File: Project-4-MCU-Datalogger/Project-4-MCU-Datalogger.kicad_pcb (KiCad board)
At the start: 2 copper layers, 51.9 x 33.4 mm, 30 parts, among them J1 Conn_01x04_Pin, J2 Conn_01x04_Pin, J3 Conn_01x09_Pin, J4 Conn_02x03_Odd_Even, U1 24LC1025, U2 24LC1025, U3 DS1337S_, U4 ATMEGA328P-AU, Y1 16 MHz, Y2 32.768 KHz

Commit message: bugfix I2C's clock signal updating routing after schematic bugfix of net label (rename from SCK to SCL)
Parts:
- removed REF**: KiCad-Logo2_5mm_SilkScreen, Symbol:KiCad-Logo2_5mm_SilkScreen
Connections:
- J1 pad 4: /SCK -> /SCL
- R3 pad 2: /SCK -> /SCL
- U1 pad 6: /SCK -> /SCL
- U2 pad 6: /SCK -> /SCL
- U3 pad 6: /SCK -> /SCL
- U4 pad 28: /SCK -> /SCL
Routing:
- net /SCL: track 0.00 -> 68.7 mm, vias 0 -> 6
- net /SCK: track 80.0 -> 16.2 mm, vias 9 -> 2
- net /SDA: track 64.0 -> 63.0 mm

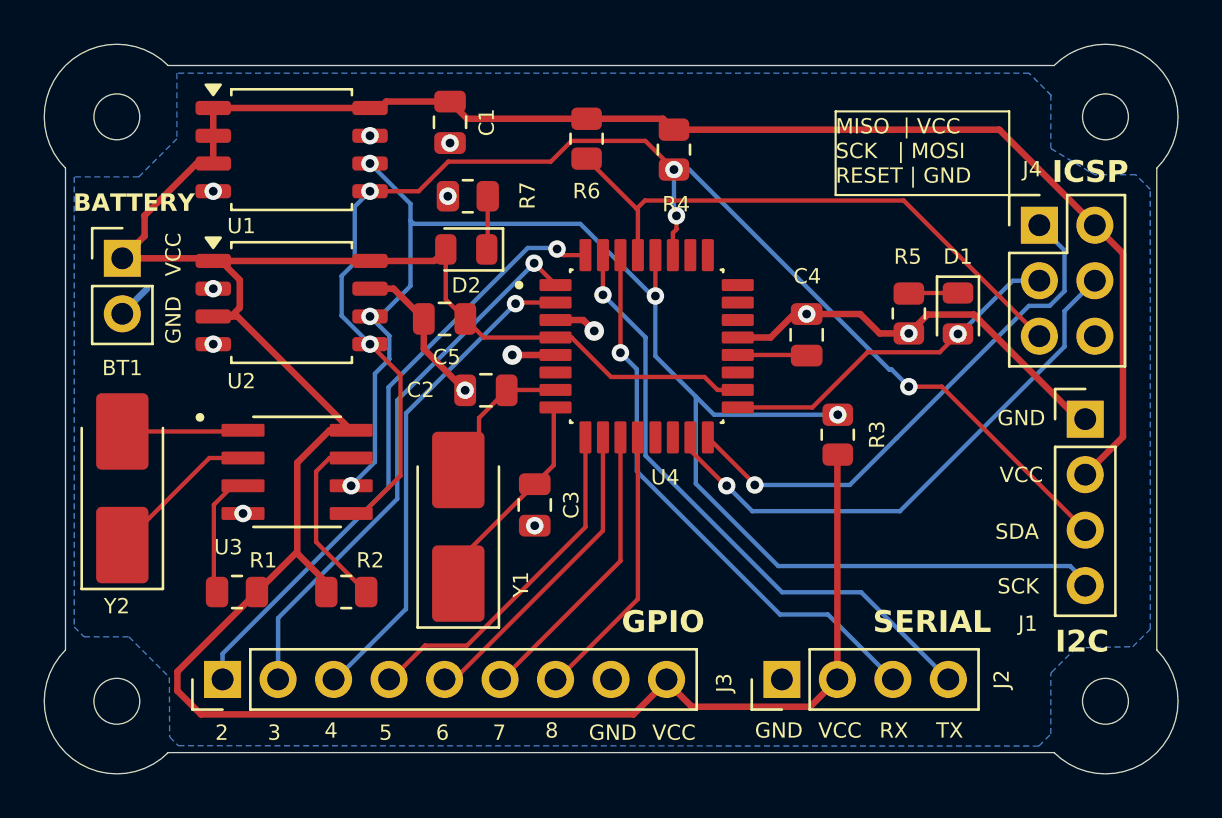
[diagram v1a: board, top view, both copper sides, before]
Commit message: delete all zones, tracks, vias before autorouting
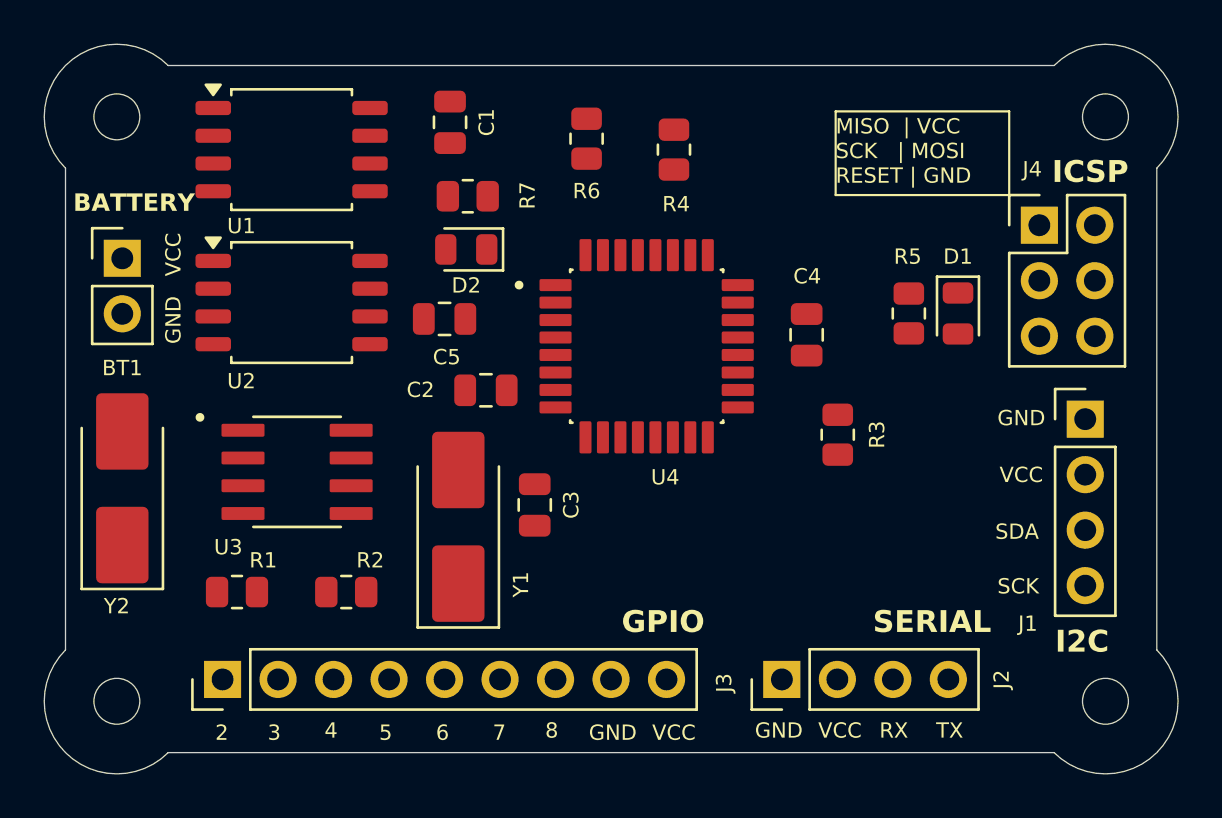
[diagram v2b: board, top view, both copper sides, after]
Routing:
- net /Vcc: track 171.1 -> 0.00 mm
- net /SCL: track 68.7 -> 0.00 mm, vias 6 -> 0
- net /SDA: track 63.0 -> 0.00 mm, vias 5 -> 0
- net GND: track 31.8 -> 0.00 mm, vias 18 -> 0
- net /D2: track 28.4 -> 0.00 mm, vias 2 -> 0
- net /TX: track 28.1 -> 0.00 mm, vias 2 -> 0
- net /RESET: track 26.6 -> 0.00 mm
- net /RX: track 25.9 -> 0.00 mm, vias 2 -> 0
- net /MOSI: track 25.6 -> 0.00 mm, vias 3 -> 0
- net /D3: track 25.4 -> 0.00 mm, vias 2 -> 0
- net /MISO: track 24.4 -> 0.00 mm, vias 2 -> 0
- net /D4: track 22.6 -> 0.00 mm, vias 2 -> 0
- net /SCK: track 16.2 -> 0.00 mm, vias 2 -> 0
- net /D5: track 16.0 -> 0.00 mm
- net /D6: track 14.4 -> 0.00 mm
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- removed copper zone on B.Cu, net GND

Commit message: autoroute with 'Freerouting' plugin (contains DRC errors)
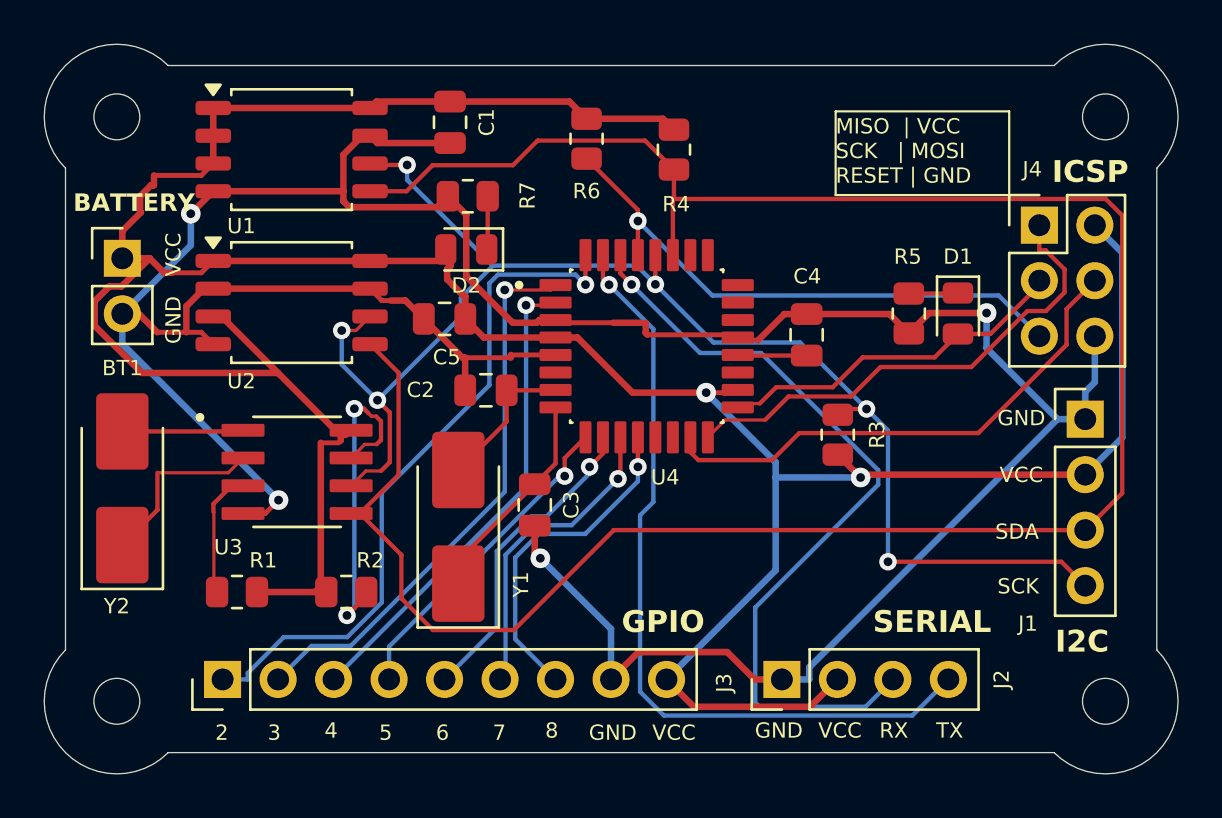
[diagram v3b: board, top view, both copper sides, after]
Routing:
- net /Vcc: track 0.00 -> 151.9 mm, vias 0 -> 2
- net GND: track 0.00 -> 142.7 mm, vias 0 -> 4
- net /SDA: track 0.00 -> 103.2 mm
- net /SCL: track 0.00 -> 66.5 mm, vias 0 -> 6
- net /TX: track 0.00 -> 36.4 mm, vias 0 -> 1
- net /RX: track 0.00 -> 36.2 mm, vias 0 -> 1
- net /D2: track 0.00 -> 31.7 mm, vias 0 -> 1
- net /RESET: track 0.00 -> 25.9 mm, vias 0 -> 1
- net /D3: track 0.00 -> 25.6 mm, vias 0 -> 1
- net /MOSI: track 0.00 -> 23.7 mm
- net /MISO: track 0.00 -> 22.8 mm
- net /D4: track 0.00 -> 22.2 mm, vias 0 -> 1
- net /SCK: track 0.00 -> 16.3 mm
- net /D8: track 0.00 -> 15.4 mm, vias 0 -> 1
- net Net-(U3-SQW/~INT): track 0.00 -> 15.1 mm, vias 0 -> 2
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
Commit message: bugfix Freerouting plugin's DRC errors (track connections issues)
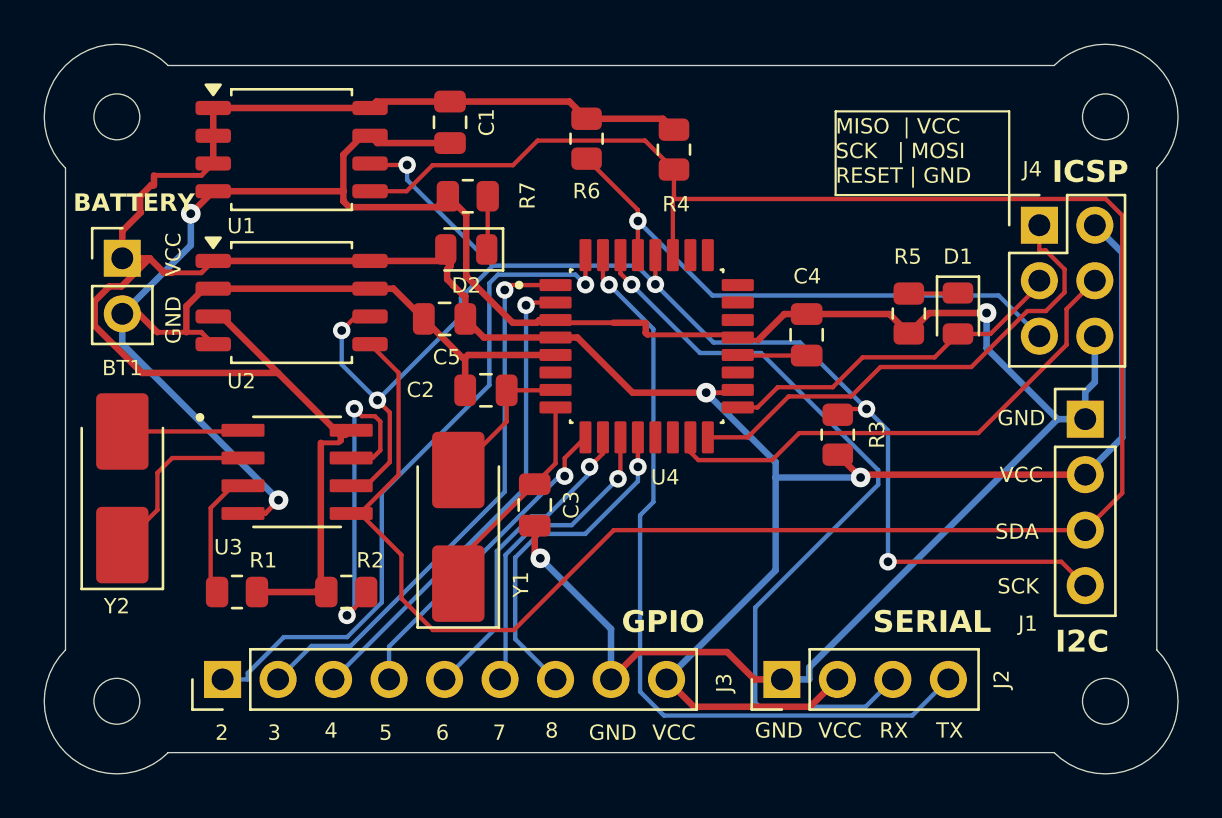
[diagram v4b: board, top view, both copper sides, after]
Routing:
- net Net-(U3-~{INTA}): track 5.89 -> 6.54 mm
